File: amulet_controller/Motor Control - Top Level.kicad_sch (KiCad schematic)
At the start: 10 parts, among them U8 DRV8353FS

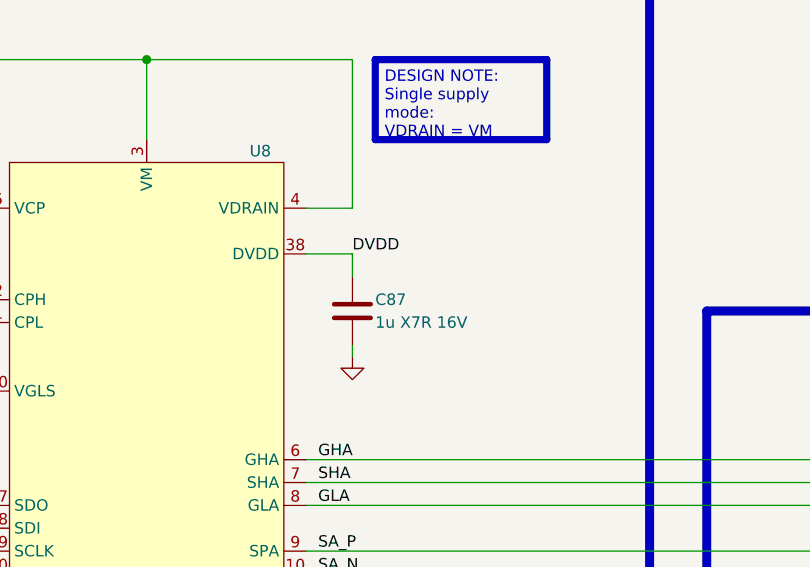
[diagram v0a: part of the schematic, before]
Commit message: filled in fields for bom, replaced inexisting components. Need to replace LEDs
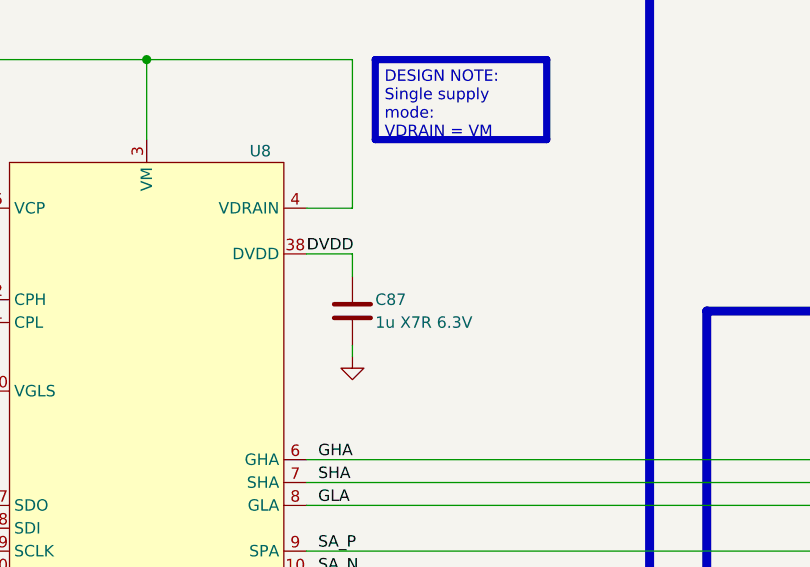
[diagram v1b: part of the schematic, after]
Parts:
- C81: footprint 0_capacitor_smd:C_0402_1005_DensitySpaced -> 0_capacitor_smd:C_0603_1608_DensityHigh; Manufacturer (none) -> Taiyo Yuden; Manufacturer Part Number (none) -> TMK107AB7105KAHT; Supplier 1 (none) -> Digikey; Supplier Part Number 1 (none) -> 587-3467-1-ND
- C82: Manufacturer (none) -> Murata Electronics; Manufacturer Part Number (none) -> GRJ31CZ72A475KE01L; Supplier 1 (none) -> Digikey; Supplier Part Number 1 (none) -> 490-GRJ31CZ72A475KE01LCT-ND
- C83: Manufacturer (none) -> Murata Electronics; Manufacturer Part Number (none) -> GCM155R71C104KA55D; Supplier 1 (none) -> Digikey; Supplier Part Number 1 (none) -> 490-4759-1-ND
- C84: footprint 0_capacitor_smd:C_0402_1005_DensityHigh -> 0_capacitor_smd:C_0603_1608_DensityHigh; Manufacturer (none) -> KEMET; Manufacturer Part Number (none) -> C0603C473K1RECAUTO; Supplier 1 (none) -> Digikey; Supplier Part Number 1 (none) -> 399-14764-1-ND
- C85: footprint 0_capacitor_smd:C_0402_1005_DensitySpaced -> 0_capacitor_smd:C_0603_1608_DensityHigh; Manufacturer (none) -> Taiyo Yuden; Manufacturer Part Number (none) -> HMK107B7104KAHT; Supplier 1 (none) -> Digikey; Supplier Part Number 1 (none) -> 587-6009-1-ND
- C86: footprint 0_capacitor_smd:C_0402_1005_DensityHigh -> 0_capacitor_smd:C_0603_1608_DensityHigh; Manufacturer (none) -> Taiyo Yuden; Manufacturer Part Number (none) -> TMK107AB7105KAHT; Supplier 1 (none) -> Digikey; Supplier Part Number 1 (none) -> 587-3467-1-ND
- C87: value 1u X7R 16V -> 1u X7R 6.3V; Manufacturer (none) -> Murata Electronics; Manufacturer Part Number (none) -> GRT155R70J105KE01D; Supplier 1 (none) -> Digikey; Supplier Part Number 1 (none) -> 490-18216-1-ND
- R7, R8: Manufacturer (none) -> Vishay; Manufacturer Part Number (none) -> ERJ-2RKF2001X; Supplier 1 (none) -> Digikey; Supplier Part Number 1 (none) -> P2.00KLCT-ND
- U8: Manufacturer (none) -> Texas Instruments; Manufacturer Part Number (none) -> DRV8353FSRTAR; Supplier 1 (none) -> Digikey; Supplier Part Number 1 (none) -> 296-DRV8353FSRTARCT-ND

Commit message: added test points
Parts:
- added TP1: GLB, 0_testpoint:TestPoint_Pad_D0.4mm_Front, symbol Connector:TestPoint
- added TP1: SA_N, 0_testpoint:TestPoint_Pad_D0.5mm_Front, symbol Connector:TestPoint
- added TP1: SC_P, 0_testpoint:TestPoint_Pad_D0.5mm_Front, symbol Connector:TestPoint
- added TP1: SC_N, 0_testpoint:TestPoint_Pad_D0.5mm_Front, symbol Connector:TestPoint
- added TP1: GLC, 0_testpoint:TestPoint_Pad_D0.4mm_Front, symbol Connector:TestPoint
- added TP1: GHC, 0_testpoint:TestPoint_Pad_D0.4mm_Front, symbol Connector:TestPoint
- added TP1: GLA, 0_testpoint:TestPoint_Pad_D0.4mm_Front, symbol Connector:TestPoint
- added TP1: SB_N, 0_testpoint:TestPoint_Pad_D0.5mm_Front, symbol Connector:TestPoint
- added TP1: GHB, 0_testpoint:TestPoint_Pad_D0.4mm_Front, symbol Connector:TestPoint
- added TP1: SA_P, 0_testpoint:TestPoint_Pad_D0.5mm_Front, symbol Connector:TestPoint
- added TP1: GHA, 0_testpoint:TestPoint_Pad_D0.4mm_Front, symbol Connector:TestPoint
- added TP1: SB_P, 0_testpoint:TestPoint_Pad_D0.5mm_Front, symbol Connector:TestPoint
- added TP1: SHB, 0_testpoint:TestPoint_Pad_D0.4mm_Front, symbol Connector:TestPoint
- added TP1: SHC, 0_testpoint:TestPoint_Pad_D0.4mm_Front, symbol Connector:TestPoint
- added TP1: SHA, 0_testpoint:TestPoint_Pad_D0.4mm_Front, symbol Connector:TestPoint
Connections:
- net GHA: now also TP1.1
- net GHB: now also TP1.1
- net GHC: now also TP1.1
- net GLA: now also TP1.1
- net GLB: now also TP1.1
- net GLC: now also TP1.1
- net SA_N: now also TP1.1
- net SA_P: now also TP1.1
- net SB_N: now also TP1.1
- net SB_P: now also TP1.1
- net SC_N: now also TP1.1
- net SC_P: now also TP1.1
- net SHA: now also TP1.1
- net SHB: now also TP1.1
- net SHC: now also TP1.1
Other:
- moved on the sheet: C81, C82, C83, C84, C85, C86, C87, R7, R8, U8

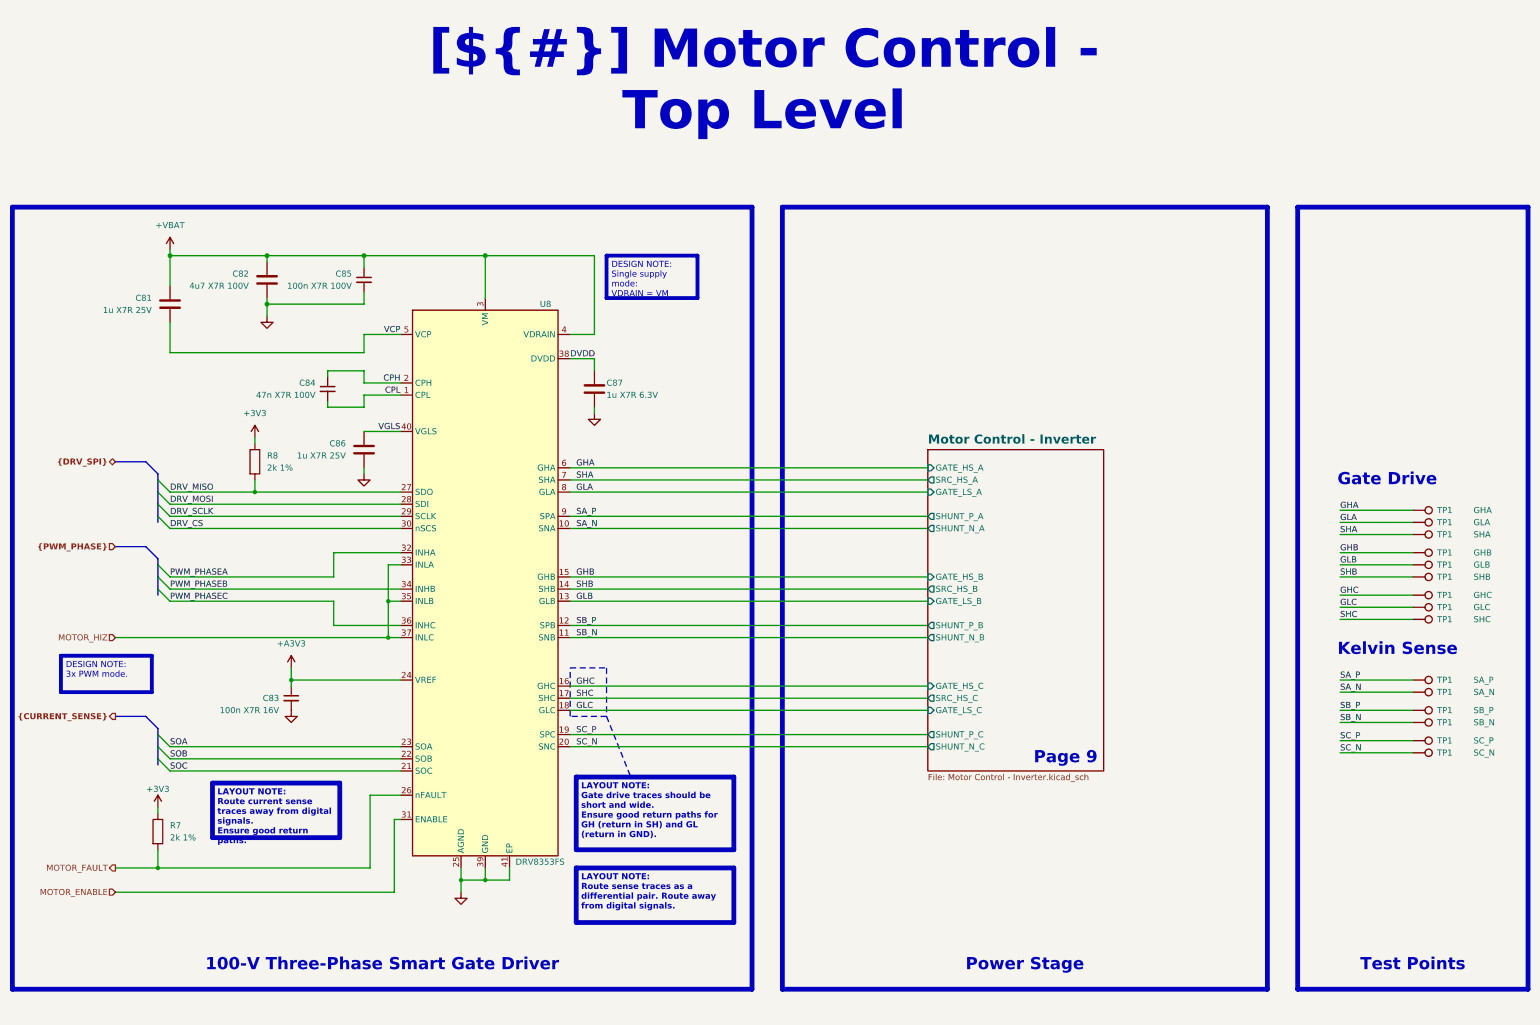
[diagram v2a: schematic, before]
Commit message: finalized pcb. TODO: add clean BOM and KiBot integration
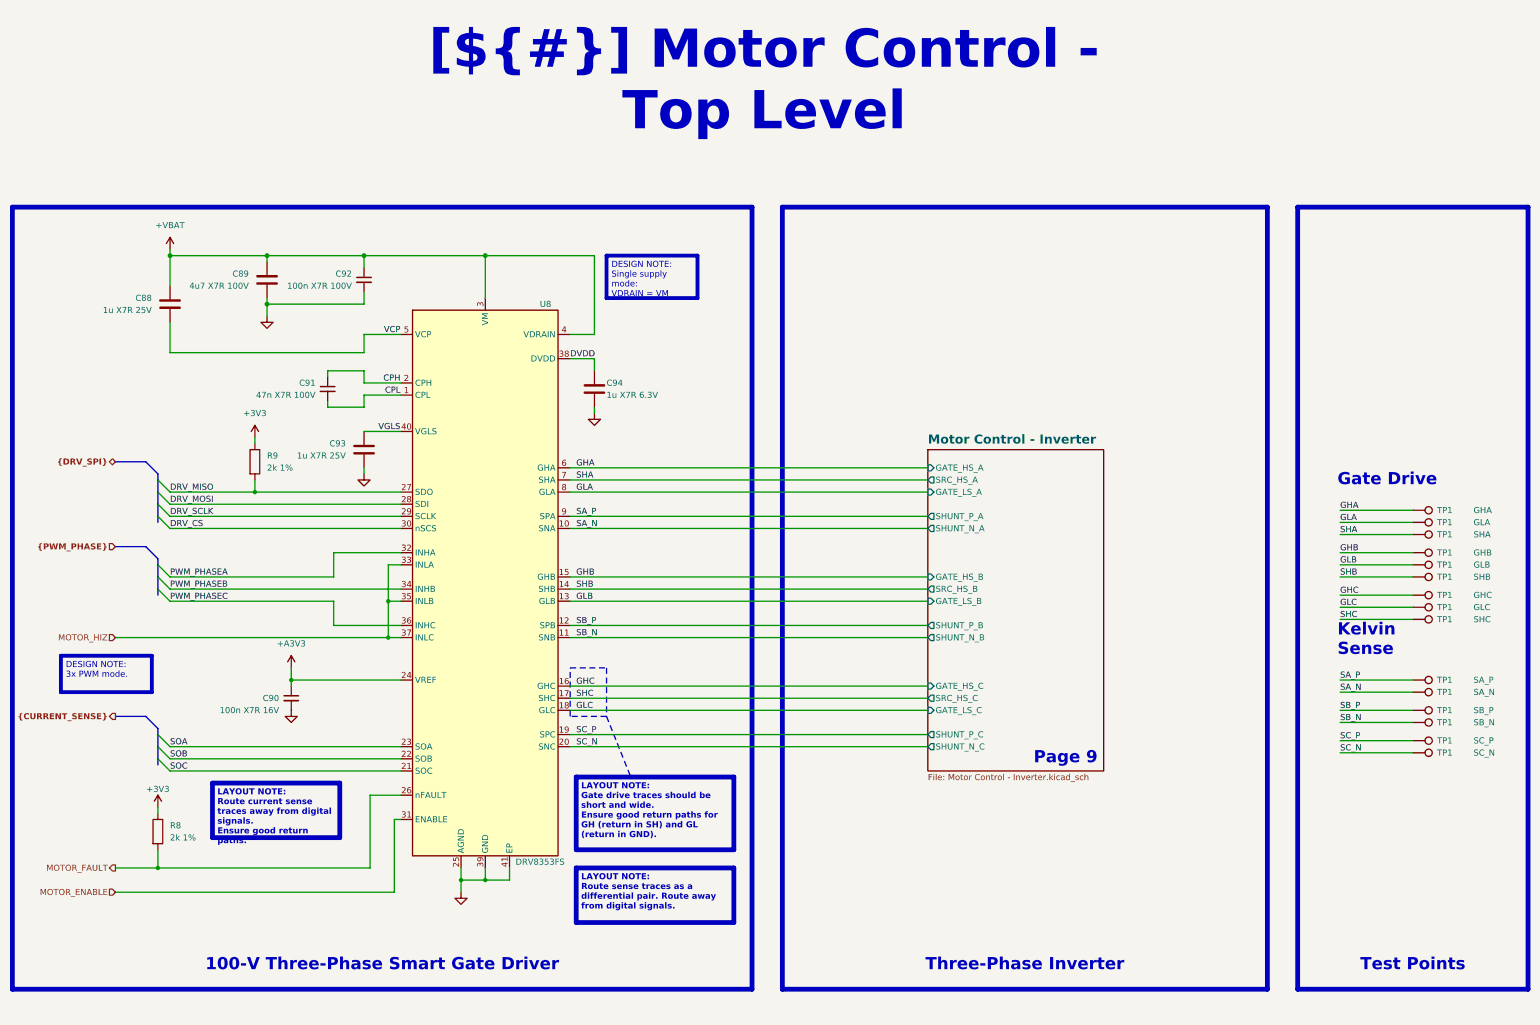
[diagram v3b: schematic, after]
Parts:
- renumbered C81 to C88, C82 to C89, C83 to C90, C84 to C91, C85 to C92, C86 to C93, C87 to C94, R7 to R8, R8 to R9

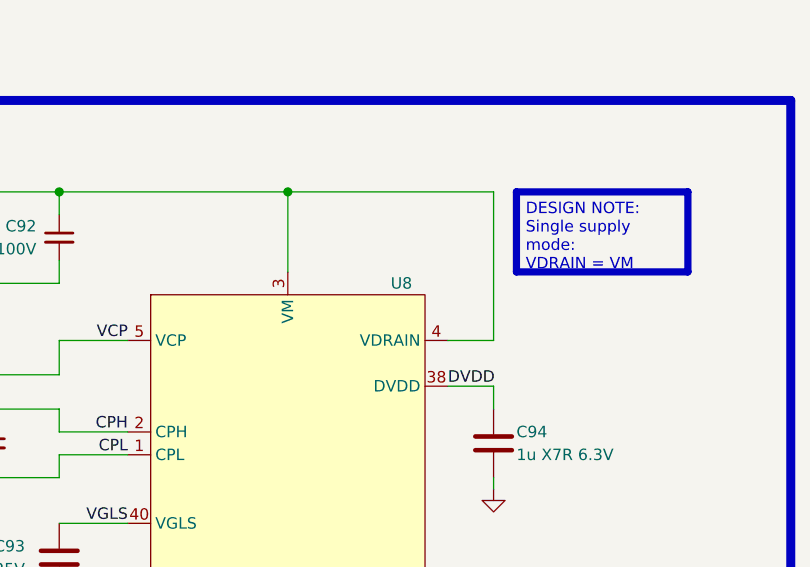
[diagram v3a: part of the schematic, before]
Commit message: corrected pcb according to reviews on reddit
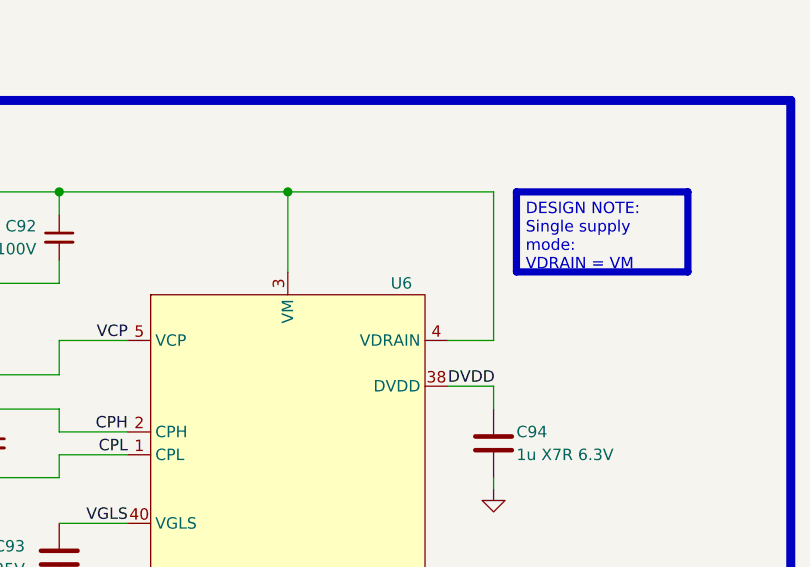
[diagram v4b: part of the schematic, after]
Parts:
- renumbered U8 to U6
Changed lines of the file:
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@@
   (symbol (lib_id "power:GND") (at 125.73 109.22 0) (unit 1)
     (in_bom yes) (on_board yes) (dnp no)
-    (property "Reference" "#PWR031" (at 125.73 115.57 0)
+    (property "Reference" "#PWR032" (at 125.73 115.57 0)
       (effects (font (size 1.27 1.27)) hide)
     )
@@
       (project "amulet_controller"
         (path "/0650c7a8-acba-429c-9f8e-eec0baf0bc1c/fede4c36-00cc-4d3d-b71c-5243ba232202/5bcbc7e4-0942-415e-ab04-e1cd42538fc3"
-          (reference "#PWR031") (unit 1)
+          (reference "#PWR032") (unit 1)
         )
       )
@@
   (symbol (lib_id "0_power_symbols:+VBAT") (at 85.09 62.23 0) (unit 1)
     (in_bom yes) (on_board yes) (dnp no) (fields_autoplaced)
-    (property "Reference" "#PWR026" (at 85.09 66.04 0)
+    (property "Reference" "#PWR027" (at 85.09 66.04 0)
       (effects (font (size 1.27 1.27)) hide)
     )
@@
       (project "amulet_controller"
         (path "/0650c7a8-acba-429c-9f8e-eec0baf0bc1c/fede4c36-00cc-4d3d-b71c-5243ba232202/5bcbc7e4-0942-415e-ab04-e1cd42538fc3"
-          (reference "#PWR026") (unit 1)
+          (reference "#PWR027") (unit 1)
         )
       )
@@
   (symbol (lib_id "0_power_symbols:+A3V3") (at 110.49 149.86 0) (unit 1)
     (in_bom yes) (on_board yes) (dnp no) (fields_autoplaced)
-    (property "Reference" "#PWR029" (at 110.49 153.67 0)
+    (property "Reference" "#PWR030" (at 110.49 153.67 0)
       (effects (font (size 1.27 1.27)) hide)
     )
@@
       (project "amulet_controller"
         (path "/0650c7a8-acba-429c-9f8e-eec0baf0bc1c/fede4c36-00cc-4d3d-b71c-5243ba232202/5bcbc7e4-0942-415e-ab04-e1cd42538fc3"
-          (reference "#PWR029") (unit 1)
+          (reference "#PWR030") (unit 1)
         )
       )
@@
   (symbol (lib_id "power:GND") (at 146.05 196.85 0) (unit 1)
     (in_bom yes) (on_board yes) (dnp no) (fields_autoplaced)
-    (property "Reference" "#PWR032" (at 146.05 203.2 0)
+    (property "Reference" "#PWR033" (at 146.05 203.2 0)
       (effects (font (size 1.27 1.27)) hide)
     )
@@
       (project "amulet_controller"
         (path "/0650c7a8-acba-429c-9f8e-eec0baf0bc1c/fede4c36-00cc-4d3d-b71c-5243ba232202/5bcbc7e4-0942-415e-ab04-e1cd42538fc3"
-          (reference "#PWR032") (unit 1)
+          (reference "#PWR033") (unit 1)
         )
       )
@@
   (symbol (lib_id "power:GND") (at 110.49 158.75 0) (unit 1)
     (in_bom yes) (on_board yes) (dnp no) (fields_autoplaced)
-    (property "Reference" "#PWR030" (at 110.49 165.1 0)
+    (property "Reference" "#PWR031" (at 110.49 165.1 0)
       (effects (font (size 1.27 1.27)) hide)
     )
@@
       (project "amulet_controller"
         (path "/0650c7a8-acba-429c-9f8e-eec0baf0bc1c/fede4c36-00cc-4d3d-b71c-5243ba232202/5bcbc7e4-0942-415e-ab04-e1cd42538fc3"
-          (reference "#PWR030") (unit 1)
+          (reference "#PWR031") (unit 1)
         )
       )
@@
   (symbol (lib_id "power:+3V3") (at 102.87 101.6 0) (unit 1)
     (in_bom yes) (on_board yes) (dnp no) (fields_autoplaced)
-    (property "Reference" "#PWR027" (at 102.87 105.41 0)
+    (property "Reference" "#PWR028" (at 102.87 105.41 0)
       (effects (font (size 1.27 1.27)) hide)
     )
@@
       (project "amulet_controller"
         (path "/0650c7a8-acba-429c-9f8e-eec0baf0bc1c/fede4c36-00cc-4d3d-b71c-5243ba232202/5bcbc7e4-0942-415e-ab04-e1cd42538fc3"
-          (reference "#PWR027") (unit 1)
+          (reference "#PWR028") (unit 1)
         )
       )
@@
   (symbol (lib_id "power:GND") (at 173.99 96.52 0) (unit 1)
     (in_bom yes) (on_board yes) (dnp no) (fields_autoplaced)
-    (property "Reference" "#PWR033" (at 173.99 102.87 0)
+    (property "Reference" "#PWR034" (at 173.99 102.87 0)
       (effects (font (size 1.27 1.27)) hide)
     )
@@
       (project "amulet_controller"
         (path "/0650c7a8-acba-429c-9f8e-eec0baf0bc1c/fede4c36-00cc-4d3d-b71c-5243ba232202/5bcbc7e4-0942-415e-ab04-e1cd42538fc3"
-          (reference "#PWR033") (unit 1)
+          (reference "#PWR034") (unit 1)
         )
       )
@@
   (symbol (lib_id "0_motor_driver:DRV8353FS") (at 151.13 170.18 0) (unit 1)
     (in_bom yes) (on_board yes) (dnp no)
-    (property "Reference" "U8" (at 162.56 73.66 0)
+    (property "Reference" "U6" (at 162.56 73.66 0)
       (effects (font (size 1.27 1.27)) (justify left))
     )
@@
       (project "amulet_controller"
         (path "/0650c7a8-acba-429c-9f8e-eec0baf0bc1c/fede4c36-00cc-4d3d-b71c-5243ba232202/5bcbc7e4-0942-415e-ab04-e1cd42538fc3"
-          (reference "U8") (unit 1)
+          (reference "U6") (unit 1)
         )
       )
@@
   (symbol (lib_id "power:+3V3") (at 82.55 179.07 0) (unit 1)
     (in_bom yes) (on_board yes) (dnp no)
-    (property "Reference" "#PWR025" (at 82.55 182.88 0)
+    (property "Reference" "#PWR026" (at 82.55 182.88 0)
       (effects (font (size 1.27 1.27)) hide)
     )
@@
       (project "amulet_controller"
         (path "/0650c7a8-acba-429c-9f8e-eec0baf0bc1c/fede4c36-00cc-4d3d-b71c-5243ba232202/5bcbc7e4-0942-415e-ab04-e1cd42538fc3"
-          (reference "#PWR025") (unit 1)
+          (reference "#PWR026") (unit 1)
         )
       )
@@
   (symbol (lib_id "power:GND") (at 105.41 76.2 0) (unit 1)
     (in_bom yes) (on_board yes) (dnp no) (fields_autoplaced)
-    (property "Reference" "#PWR028" (at 105.41 82.55 0)
+    (property "Reference" "#PWR029" (at 105.41 82.55 0)
       (effects (font (size 1.27 1.27)) hide)
     )
@@
       (project "amulet_controller"
         (path "/0650c7a8-acba-429c-9f8e-eec0baf0bc1c/fede4c36-00cc-4d3d-b71c-5243ba232202/5bcbc7e4-0942-415e-ab04-e1cd42538fc3"
-          (reference "#PWR028") (unit 1)
-        )
-      )
+          (reference "#PWR029") (unit 1)
+        )
+      )
